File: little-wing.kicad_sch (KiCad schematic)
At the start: 72 parts, among them IC1 AP7335-WG-7, J1 nice!view, J2 Battery, J3 trackball, J4 trackball, SW1 Power, SW2 Reset, U1 nice!nano v2, U2 PMW3610

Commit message: Wiring up the MCU block
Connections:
- net CS_D: now also U1.7 (4); no longer U1.8 (5)
- net CS_T: now also U1.8 (5); no longer U1.7 (4)
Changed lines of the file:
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@@
+		)
+	)
+	(global_label "CS_T"
+		(shape input)
+		(at 35.56 41.91 180)
+		(fields_autoplaced yes)
+		(effects
+			(font
+				(size 1.27 1.27)
+			)
+			(justify right)
+		)
+		(property "Intersheetrefs" "${INTERSHEET_REFS}"
+			(at 28.1601 41.91 0)
+			(effects
+				(font
+					(size 1.27 1.27)
+				)
+				(justify right)
+				(hide yes)
+			)
 		)
 	)
@@
 		)
 	)
+	(global_label "CS_D"
+		(shape input)
+		(at 35.56 39.37 180)
+		(fields_autoplaced yes)
+		(effects
+			(font
+				(size 1.27 1.27)
+			)
+			(justify right)
+		)
+		(property "Intersheetrefs" "${INTERSHEET_REFS}"
+			(at 27.8577 39.37 0)
+			(effects
+				(font
+					(size 1.27 1.27)
+				)
+				(justify right)
+				(hide yes)
+			)
+		)
+	)
 	(global_label "GND"
 		(shape input)
@@
 		)
 	)
-	(global_label "CS_D"
-		(shape input)
-		(at 35.56 41.91 180)
-		(fields_autoplaced yes)
-		(effects
-			(font
-				(size 1.27 1.27)
-			)
-			(justify right)
-		)
-		(property "Intersheetrefs" "${INTERSHEET_REFS}"
-			(at 27.8577 41.91 0)
-			(effects
-				(font
-					(size 1.27 1.27)
-				)
-				(justify right)
-				(hide yes)
-			)
-		)
-	)
 	(global_label "Row 0"
 		(shape input)
@@
 			(effects
 				(font
-					(size 1.27 1.27)
-				)
-				(justify right)
-				(hide yes)
-			)
-		)
-	)
-	(global_label "CS_T"
-		(shape input)
-		(at 35.56 39.37 180)
-		(fields_autoplaced yes)
-		(effects
-			(font
-				(size 1.27 1.27)
-			)
-			(justify right)
-		)
-		(property "Intersheetrefs" "${INTERSHEET_REFS}"
-			(at 28.1601 39.37 0)
-			(effects
-				(font

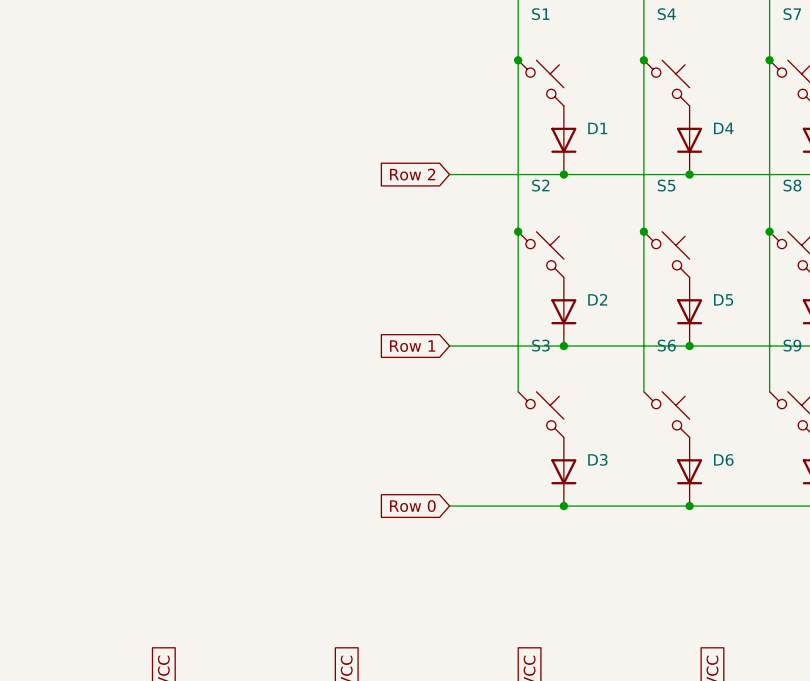
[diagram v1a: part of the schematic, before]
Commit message: Attaching the columns to MCU
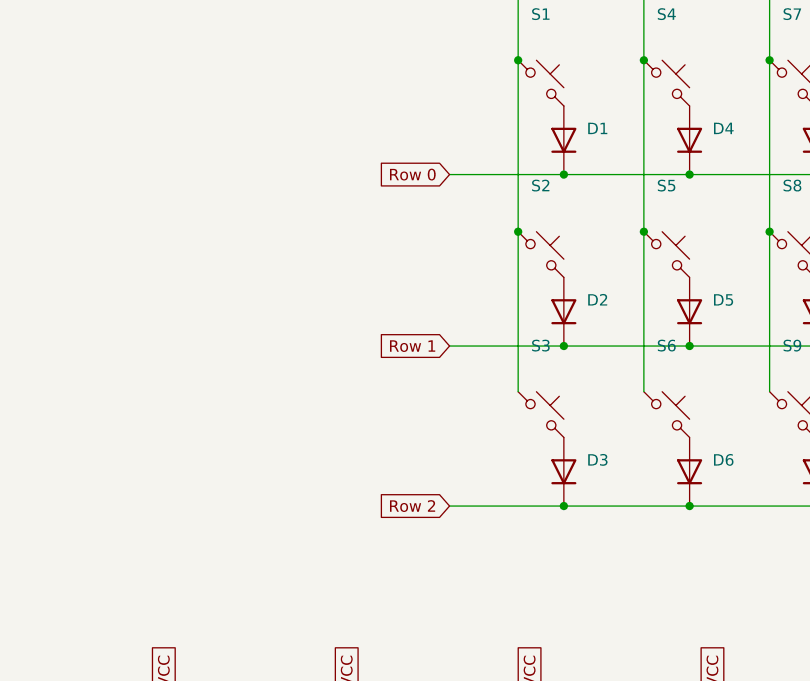
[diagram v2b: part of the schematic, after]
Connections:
- net Row 0: now also D1.1 (K), D10.1 (K), D13.1 (K), D16.1 (K), D4.1 (K), D7.1 (K); no longer D12.1 (K), D15.1 (K), D3.1 (K), D6.1 (K), D9.1 (K)
- net Row 2: now also D12.1 (K), D15.1 (K), D3.1 (K), D6.1 (K), D9.1 (K); no longer D1.1 (K), D10.1 (K), D13.1 (K), D16.1 (K), D4.1 (K), D7.1 (K)

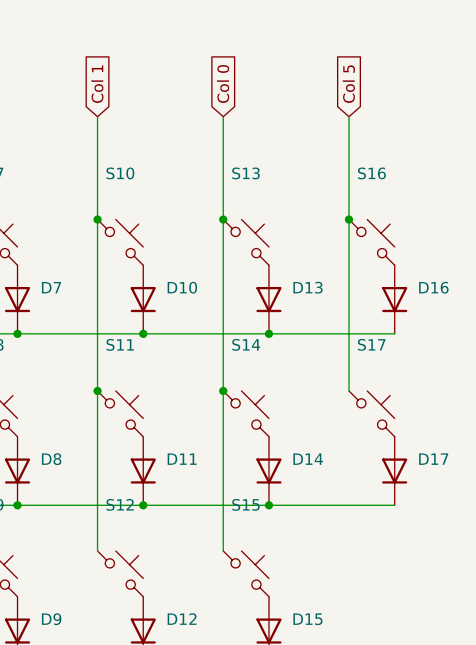
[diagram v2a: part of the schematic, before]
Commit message: Wiring together the thumbs cluster
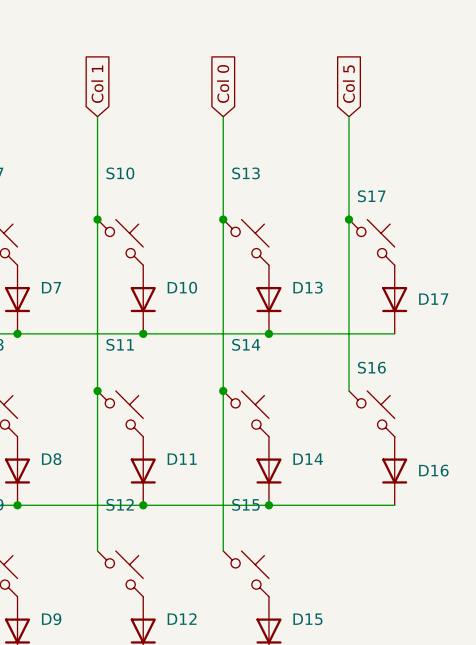
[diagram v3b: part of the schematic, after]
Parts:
- renumbered D17 to D16, D16 to D17, S17 to S16, S16 to S17
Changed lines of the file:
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@@
 		(dnp no)
 		(fields_autoplaced yes)
-		(property "Reference" "S17"
-			(at 270.51 53.34 0)
+		(property "Reference" "S16"
+			(at 270.51 55.88 0)
 			(effects
 				(font
@@
 			(project "little-wing"
 				(path "/3a835e6f-a660-4b38-a102-87841cdd95ed"
-					(reference "S17")
+					(reference "S16")
 					(unit 1)
 				)
@@
 		(dnp no)
 		(fields_autoplaced yes)
-		(property "Reference" "D16"
-			(at 275.59 46.9899 90)
+		(property "Reference" "D17"
+			(at 275.59 48.2599 90)
 			(effects
 				(font
@@
 			(project "little-wing"
 				(path "/3a835e6f-a660-4b38-a102-87841cdd95ed"
-					(reference "D16")
+					(reference "D17")
 					(unit 1)
 				)
@@
 		(dnp no)
 		(fields_autoplaced yes)
-		(property "Reference" "S16"
-			(at 270.51 34.29 0)
+		(property "Reference" "S17"
+			(at 270.51 36.83 0)
 			(effects
 				(font
@@
 			(project "little-wing"
 				(path "/3a835e6f-a660-4b38-a102-87841cdd95ed"
-					(reference "S16")
+					(reference "S17")
 					(unit 1)
 				)
@@
 		(dnp no)
 		(fields_autoplaced yes)
-		(property "Reference" "D17"
-			(at 275.59 66.0399 90)
+		(property "Reference" "D16"
+			(at 275.59 67.3099 90)
 			(effects
 				(font
@@
 			(project "little-wing"
 				(path "/3a835e6f-a660-4b38-a102-87841cdd95ed"
-					(reference "D17")
+					(reference "D16")
 					(unit 1)
 				)

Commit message: Adding the left/right hand split
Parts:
- added D35, D36, D37, D38, D39, D40, D41, D42, D43, D44, D45, D46, D47, D48, D49, D50, D51: Diode, ScottoKeebs_Components:Diode_SOD-123_Reversible, symbol ScottoKeebs:Placeholder_Diode
- added D52, D53, D54, D55, D56, D57, D58, D59, D60, D61, D62, D63, D64, D65, D66, D67, D68: LED_SK6812MINI, ScottoKeebs_Components:LED_SK6812MINI_Reversible, symbol ScottoKeebs:LED_SK6812MINI
- added J5: trackball, Connector_Wuerth:Wuerth_WR-WTB_64800611622_1x06_P1.50mm_Vertical, symbol Connector:Conn_01x06_Socket
- added J6: nice!view, Connector_PinHeader_2.54mm:PinHeader_1x05_P2.54mm_Vertical, symbol Connector:Conn_01x05_Socket
- added J7: Battery, Connector_JST:JST_ZH_S2B-ZR-SM4A-TF_1x02-1MP_P1.50mm_Horizontal_Reversible, symbol Connector_Generic:Conn_01x02
- added S18, S19, S20, S21, S22, S23, S24, S25, S26, S27, S28, S29, S30, S31, S32, S33, S34: Keyswitch, keyswitches:Kailh_socket_PG1350_reversible_better, symbol ScottoKeebs:Placeholder_Keyswitch
- added SW3: Reset, Button_Switch_SMD:SW_SPST_B3U-1000P_Reversible, symbol ScottoKeebs:Placeholder_Switch
- added SW4: Power, Button_Switch_SMD:SW_SPDT_PCM12_Reversible, symbol ScottoKeebs:Placeholder_Switch
- added U3: nice!nano v2, keyboard_reversible:ProMicro, symbol ScottoKeebs:MCU_Nice_Nano_V2
- J4: value trackball -> rotary
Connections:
- net GND: now also J7.1 (Pin_1), SW3.1; no longer D18.3 (GND), D19.3 (GND), D20.3 (GND), D21.3 (GND), D22.3 (GND), D23.3 (GND), D24.3 (GND), D25.3 (GND), D26.3 (GND), D27.3 (GND), D28.3 (GND), D29.3 (GND), D30.3 (GND), D31.3 (GND), D32.3 (GND), D33.3 (GND), D34.3 (GND), J1.4 (Pin_4), J4.6 (Pin_6), U1.23 (GND), U1.3 (GND), U1.4 (GND)
- net RGB: now also D68.4 (DIN); no longer D34.4 (DIN), U1.1
- net BAT renamed BAT L
- net CS_D renamed CS_D L
- net CS_T renamed CS_T  L
- net CS_T  L: no longer U1.8 (5)
- net Col 0 renamed Col 0 L
- net Col 1 renamed Col 1 L
- net Col 2 renamed Col 2 L
- net Col 3 renamed Col 3 L
- net Col 4 renamed Col 4 L
- net Col 5 renamed Col 5 L
- net MISO renamed MISO L
- net MOSI renamed MOSI L
- net RESET renamed RST L
- net Row 0 renamed Row 0 L
- net Row 1 renamed Row 1 L
- net Row 2 renamed Row 2 L
- net SCK renamed SCK L
- net SCK L: no longer J4.4 (Pin_4)
- net VCC renamed VCC L
- new net: D62.4 (DIN), D63.2 (DOUT)
- new net: D63.4 (DIN), D64.2 (DOUT)
- new net: D53.4 (DIN), D54.2 (DOUT)
- new net: D54.4 (DIN), D55.2 (DOUT)
- new net: D43.2 (A), S26.2
- new net: D45.2 (A), S28.2
- new net: D47.2 (A), S30.2
- new net: D50.2 (A), S33.2
- new net: D46.2 (A), S29.2
- new net: D41.2 (A), S24.2
- new net: J7.2 (Pin_2), SW4.1
- new net: D37.2 (A), S20.2
- new net: D64.4 (DIN), D65.2 (DOUT)
- new net: D65.4 (DIN), D66.2 (DOUT)
- new net: D66.4 (DIN), D67.2 (DOUT)
- new net: D39.2 (A), S22.2
- new net: D61.4 (DIN), D62.2 (DOUT)
- new net: D52.4 (DIN), D53.2 (DOUT)
- new net: D35.2 (A), S18.2
- new net: D40.2 (A), S23.2
- new net: D44.2 (A), S27.2
- new net: D38.2 (A), S21.2
- new net: D55.4 (DIN), D56.2 (DOUT)
- new net: D56.4 (DIN), D57.2 (DOUT)
- new net: D48.2 (A), S31.2
- new net: D60.4 (DIN), D61.2 (DOUT)
- new net: D59.4 (DIN), D60.2 (DOUT)
- new net: D36.2 (A), S19.2
- new net: D67.4 (DIN), D68.2 (DOUT)
- new net: D57.4 (DIN), D58.2 (DOUT)
- new net: D58.4 (DIN), D59.2 (DOUT)
- new net: D42.2 (A), S25.2
- new net: D49.2 (A), S32.2
- new net: D51.2 (A), S34.2
- new net BAT R: SW4.2, U3.24 (B+)
- new net CS_D R: J6.5 (Pin_5), U3.7 (4)
- new net CS_T L: U1.8 (5)
- new net CS_T R: J5.2 (Pin_2), U3.8 (5)
- new net Col 0 R: S30.1, S31.1, S32.1, U3.20 (21)
- new net Col 1 R: S27.1, S28.1, S29.1, U3.19 (20)
- new net Col 2 R: S24.1, S25.1, S26.1, U3.18 (19)
- new net Col 3 R: S21.1, S22.1, S23.1, U3.17 (18)
- new net Col 4 R: S18.1, S19.1, S20.1, U3.16 (15)
- new net Col 5 R: S33.1, S34.1, U3.15 (14)
- new net GND L: D18.3 (GND), D19.3 (GND), D20.3 (GND), D21.3 (GND), D22.3 (GND), D23.3 (GND), D24.3 (GND), D25.3 (GND), D26.3 (GND), D27.3 (GND), D28.3 (GND), D29.3 (GND), D30.3 (GND), D31.3 (GND), D32.3 (GND), D33.3 (GND), D34.3 (GND), J1.4 (Pin_4), J4.6 (Pin_6), U1.23 (GND), U1.3 (GND), U1.4 (GND)
- new net GND R: D52.3 (GND), D53.3 (GND), D54.3 (GND), D55.3 (GND), D56.3 (GND), D57.3 (GND), D58.3 (GND), D59.3 (GND), D60.3 (GND), D61.3 (GND), D62.3 (GND), D63.3 (GND), D64.3 (GND), D65.3 (GND), D66.3 (GND), D67.3 (GND), D68.3 (GND), J5.6 (Pin_6), J6.4 (Pin_4), U3.23 (GND), U3.3 (GND), U3.4 (GND)
- new net MISO R: J5.5 (Pin_5), U3.6 (3)
- new net MOSI R: J5.3 (Pin_3), J6.1 (Pin_1), U3.5 (2)
- new net RGB L: D34.4 (DIN), U1.1
- new net RGB R: U3.1
- new net RST R: SW3.2, U3.22 (RST)
- new net Row 0 R: D35.1 (K), D38.1 (K), D41.1 (K), D44.1 (K), D47.1 (K), D50.1 (K), U3.9 (6)
- new net Row 1 R: D36.1 (K), D39.1 (K), D42.1 (K), D45.1 (K), D48.1 (K), D51.1 (K), U3.10 (7)
- new net Row 2 R: D37.1 (K), D40.1 (K), D43.1 (K), D46.1 (K), D49.1 (K), U3.11 (8)
- new net SCK  L: J4.4 (Pin_4)
- new net SCK R: J5.4 (Pin_4), J6.2 (Pin_2), U3.2 (0)
- new net VCC R: D52.1 (VSS), D53.1 (VSS), D54.1 (VSS), D55.1 (VSS), D56.1 (VSS), D57.1 (VSS), D58.1 (VSS), D59.1 (VSS), D60.1 (VSS), D61.1 (VSS), D62.1 (VSS), D63.1 (VSS), D64.1 (VSS), D65.1 (VSS), D66.1 (VSS), D67.1 (VSS), D68.1 (VSS), J5.1 (Pin_1), J6.3 (Pin_3), U3.21 (3.3v)
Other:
- note added: "Left side"
- note added: "Right side"
- note added: "Trackball unit"
- moved on the sheet: C1, C10, C11, C2, C3, C6, C7, C8, C9, D1, D10, D11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

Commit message: Syncing the schematics and pcb
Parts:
- removed D51: Diode, ScottoKeebs_Components:Diode_SOD-123_Reversible, symbol ScottoKeebs:Placeholder_Diode
- removed S34: Keyswitch, keyswitches:Kailh_socket_PG1350_reversible_better, symbol ScottoKeebs:Placeholder_Keyswitch
- D1, D10, D11, D12, D13, D14, D15, D16, D17, D2, D3, D35, D36, D37, D38, D39, D4, D40, D41, D42, D43, D44, D45, D46, D47, D48, D49, D5, D50, D6, D7, D8, D9: footprint ScottoKeebs_Components:Diode_SOD-123_Reversible -> ScottoKeebs_Components:Diode_SOD-123
- D18, D19, D20, D21, D22, D23, D24, D25, D26, D27, D28, D29, D30, D31, D32, D33, D34, D52, D53, D54, D55, D56, D57, D58, D59, D60, D61, D62, D63, D64, D65, D66, D67, D68: footprint ScottoKeebs_Components:LED_SK6812MINI_Reversible -> ScottoKeebs_Components:LED_SK6812MINI
- J2, J7: footprint Connector_JST:JST_ZH_S2B-ZR-SM4A-TF_1x02-1MP_P1.50mm_Horizontal_Reversible -> Connector_JST:JST_ZH_S2B-ZR-SM4A-TF_1x02-1MP_P1.50mm_Horizontal
- S1, S10, S11, S12, S13, S14, S15, S16, S17, S18, S19, S2, S20, S21, S22, S23, S24, S25, S26, S27, S28, S29, S3, S30, S31, S32, S33, S4, S5, S6, S7, S8, S9: footprint keyswitches:Kailh_socket_PG1350_reversible_better -> keyswitches:Kailh_socket_PG1350
- SW1, SW4: footprint Button_Switch_SMD:SW_SPDT_PCM12_Reversible -> Button_Switch_SMD:SW_SPDT_PCM12
- SW2, SW3: footprint Button_Switch_SMD:SW_SPST_B3U-1000P_Reversible -> Button_Switch_SMD:SW_SPST_B3U-1000P
- U1, U3: footprint keyboard_reversible:ProMicro -> ScottoKeebs_MCU:Nice_Nano_V2_Flipped
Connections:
- net RGB is gone; now on net RGB R: D68.4 (DIN)
- net GND: no longer J2.1 (Pin_1), J7.1 (Pin_1), SW2.1, SW3.1
- net GND L: now also J2.1 (Pin_1), SW2.1
- net GND R: now also J7.1 (Pin_1), SW3.1

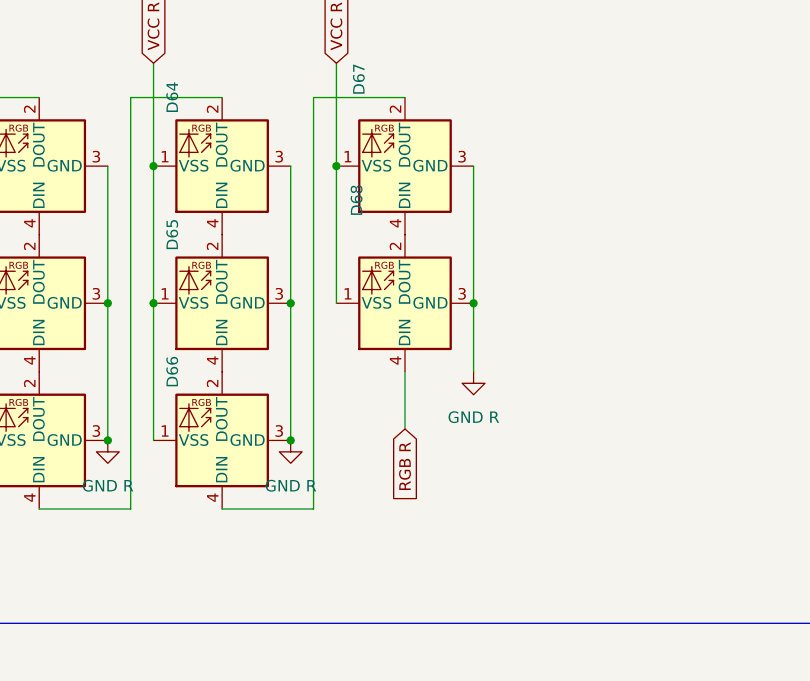
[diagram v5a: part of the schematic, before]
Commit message: Creating the reusable key pad
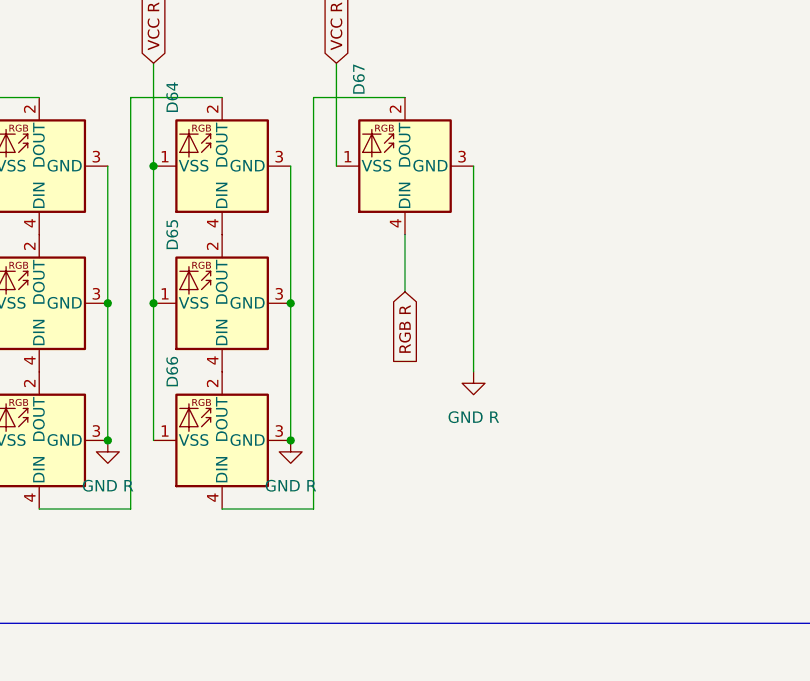
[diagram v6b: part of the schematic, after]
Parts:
- removed D68: LED_SK6812MINI, ScottoKeebs_Components:LED_SK6812MINI, symbol ScottoKeebs:LED_SK6812MINI
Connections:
- net RGB R: now also D67.4 (DIN)
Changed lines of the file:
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@@
 	)
 	(junction
-		(at 359.41 138.43)
-		(diameter 0)
-		(color 0 0 0 0)
-	)
-	(junction
 		(at 176.53 50.8)
 		(diameter 0)
@@
 	)
 	(junction
-		(at 344.17 123.19)
-		(diameter 0)
-		(color 0 0 0 0)
-	)
-	(junction
 		(at 90.17 191.77)
 		(diameter 0)
@@
 	(wire
 		(pts
-			(xy 359.41 146.05) (xy 359.41 138.43)
-		)
-		(stroke
-			(width 0)
-			(type default)
-		)
-	)
-	(wire
-		(pts
 			(xy 106.68 207.01) (xy 110.49 207.01)
 		)
@@
 	(wire
 		(pts
-			(xy 344.17 123.19) (xy 344.17 138.43)
-		)
-		(stroke
-			(width 0)
-			(type default)
-		)
-	)
-	(wire
-		(pts
 			(xy 148.59 66.04) (xy 162.56 66.04)
 		)
@@
 	(wire
 		(pts
-			(xy 351.79 152.4) (xy 351.79 146.05)
+			(xy 351.79 137.16) (xy 351.79 130.81)
 		)
 		(stroke
@@
 	(wire
 		(pts
-			(xy 359.41 123.19) (xy 359.41 138.43)
+			(xy 359.41 123.19) (xy 359.41 146.05)
 		)
 		(stroke
@@
 	(global_label "RGB R"
 		(shape input)
-		(at 351.79 152.4 270)
+		(at 351.79 137.16 270)
 		(fields_autoplaced yes)
 		(effects
@@
 		)
 		(property "Intersheetrefs" "${INTERSHEET_REFS}"
-			(at 351.79 161.4328 90)
+			(at 351.79 146.1928 90)
 			(effects
 				(font
@@
 					(unit 1)
 				)
-			)
-		)
-	)
-	(symbol
-		(lib_id "ScottoKeebs:LED_SK6812MINI")
-		(at 351.79 138.43 180)
-		(unit 1)
-		(exclude_from_sim no)
-		(in_bom yes)
-		(on_board yes)
-		(dnp no)
-		(property "Reference" "D68"
-			(at 346.456 127 90)
-			(effects
-				(font
-					(size 1.27 1.27)
-				)
-			)
-		)
-		(property "Value" "LED_SK6812MINI"
-			(at 348.8338 124.46 90)
-			(effects
-				(font
-					(size 1.27 1.27)
-				)
-				(hide yes)
-			)
-		)
-		(property "Footprint" "ScottoKeebs_Components:LED_SK6812MINI"
-			(at 350.52 130.81 0)
-			(effects
-				(font
-					(size 1.27 1.27)
-				)
-				(justify left top)
-				(hide yes)
-			)
-		)
-		(property "Datasheet" "https://cdn-shop.adafruit.com/product-files/2686/SK6812MINI_REV.01-1-2.pdf"
-			(at 349.25 128.905 0)
-			(effects
-				(font
-					(size 1.27 1.27)
-				)
-				(justify left top)
-				(hide yes)
-			)
-		)
-		(property "Description" "RGB LED with integrated controller"
-			(at 351.79 138.43 0)
-			(effects
-				(font
-					(size 1.27 1.27)
-				)
-				(hide yes)
-			)
-		)
-		(pin "2"
-		)
-		(pin "4"
-		)
-		(pin "3"
-		)
-		(pin "1"
-		)
-		(instances
-			(project "little-wing"
-				(path "/3a835e6f-a660-4b38-a102-87841cdd95ed"
-					(reference "D68")
-					(unit 1)
-				)
